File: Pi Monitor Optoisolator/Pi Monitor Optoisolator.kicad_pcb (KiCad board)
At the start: 2 copper layers, 38 x 38 mm, 15 parts, among them J1 Conn_01x07_Pin, J2 Conn_01x07_Pin, Q1 WL-OCPT_SERIES_827, Q2 WL-OCPT_SERIES_827, Q3 WL-OCPT_SERIES_827

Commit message: Minor adjustments
* Renamed LICENSE to COPYING (I wish GitHub would ask you what you wanted to name the license file)
* Added a COPYRIGHT NOTICE for the Pi Monitor Optoisolator. I did this as a seperate file, because unlike actual code files, there's not a ton of room for lots of text in a schematic or PCB drawing file.
* Update .gitignore file
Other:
- board text added: "Pi Monitor Optoisolator PCB v1.0 Part of mcu-on-the-go project https://github.com/jseyfert3/mcu-on-the-go"
- board text removed: "Pi Monitor Optoisolator Board v1.0 github.com/jseyfert3/"
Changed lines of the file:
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@@
 	)
 	(paper "A4")
+	(title_block
+		(title "Pi Monitor Optoisolator PCB")
+		(date "2025-07-18")
+		(rev "v1.0")
+		(comment 1 "See details at https://github.com/jseyfert3/mcu-on-the-go")
+		(comment 2 "Released under GPL-3.0-or-later license")
+		(comment 3 "Copyright 2025 Jonathan Seyfert")
+	)
 	(layers
 		(0 "F.Cu" signal)
@@
 		(property ki_fp_filters "R_*")
 		(sheetname "/")
-		(sheetfile "Pi_monitor.kicad_sch")
+		(sheetfile "Pi Monitor Optoisolator.kicad_sch")
 		(attr through_hole)
 		(fp_line
@@
 		(property ki_fp_filters "Connector*:*_1x??_*")
 		(sheetname "/")
-		(sheetfile "Pi_monitor.kicad_sch")
+		(sheetfile "Pi Monitor Optoisolator.kicad_sch")
 		(attr through_hole)
 		(fp_line
@@
 		)
 		(sheetname "/")
-		(sheetfile "Pi_monitor.kicad_sch")
+		(sheetfile "Pi Monitor Optoisolator.kicad_sch")
 		(attr through_hole)
 		(fp_line
@@
 		(property ki_fp_filters "Connector*:*_1x??_*")
 		(sheetname "/")
-		(sheetfile "Pi_monitor.kicad_sch")
+		(sheetfile "Pi Monitor Optoisolator.kicad_sch")
 		(attr through_hole)
 		(fp_line
@@
 		(property ki_fp_filters "R_*")
 		(sheetname "/")
-		(sheetfile "Pi_monitor.kicad_sch")
+		(sheetfile "Pi Monitor Optoisolator.kicad_sch")
 		(attr through_hole)
 		(fp_line
@@
 		)
 		(sheetname "/")
-		(sheetfile "Pi_monitor.kicad_sch")
+		(sheetfile "Pi Monitor Optoisolator.kicad_sch")
 		(attr through_hole)
 		(fp_line
@@
 		(property ki_fp_filters "R_*")
 		(sheetname "/")
-		(sheetfile "Pi_monitor.kicad_sch")
+		(sheetfile "Pi Monitor Optoisolator.kicad_sch")
 		(attr through_hole)
 		(fp_line
@@
 		)
 		(sheetname "/")
-		(sheetfile "Pi_monitor.kicad_sch")
+		(sheetfile "Pi Monitor Optoisolator.kicad_sch")
 		(attr through_hole)
 		(fp_line
@@
 		(property ki_fp_filters "R_*")
 		(sheetname "/")
-		(sheetfile "Pi_monitor.kicad_sch")
+		(sheetfile "Pi Monitor Optoisolator.kicad_sch")
 		(attr through_hole)
 		(fp_line
@@
 		(property ki_fp_filters "R_*")
 		(sheetname "/")
-		(sheetfile "Pi_monitor.kicad_sch")
+		(sheetfile "Pi Monitor Optoisolator.kicad_sch")
 		(attr through_hole)
 		(fp_line
@@
 		(property ki_fp_filters "R_*")
 		(sheetname "/")
-		(sheetfile "Pi_monitor.kicad_sch")
+		(sheetfile "Pi Monitor Optoisolator.kicad_sch")
 		(attr through_hole)
 		(fp_line
@@
 		(layer "Edge.Cuts")
 	)
-	(gr_text "Pi Monitor Optoisolator Board\nv1.0\n\ngithub.com/jseyfert3/"
-		(at 76.29 78.21 0)
+	(gr_text "Pi Monitor Optoisolator PCB\nv1.0\n\nPart of mcu-on-the-go project\nhttps://github.com/jseyfert3/mcu-on-the-go"
+		(at 84.74 79.01 0)
 		(layer "B.SilkS")
 		(effects
 			(font
 				(size 1 1)
-				(thickness 0.1)
+				(thickness 0.127)
 			)
 			(justify left bottom mirror)

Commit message: fix: Updated PN of optoisolator
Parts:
- Q1, Q2, Q3: value WL-OCPT_SERIES_827 -> 140827181010
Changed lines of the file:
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@@
 			)
 		)
-		(property "Value" "WL-OCPT_SERIES_827"
+		(property "Value" "140827181010"
 			(at 0 7.365 0)
 			(layer "F.Fab")
@@
 			)
 		)
-		(property "Value" "WL-OCPT_SERIES_827"
+		(property "Value" "140827181010"
 			(at 0 7.365 0)
 			(layer "F.Fab")
@@
 			)
 		)
-		(property "Value" "WL-OCPT_SERIES_827"
+		(property "Value" "140827181010"
 			(at 0 7.365 0)
 			(layer "F.Fab")

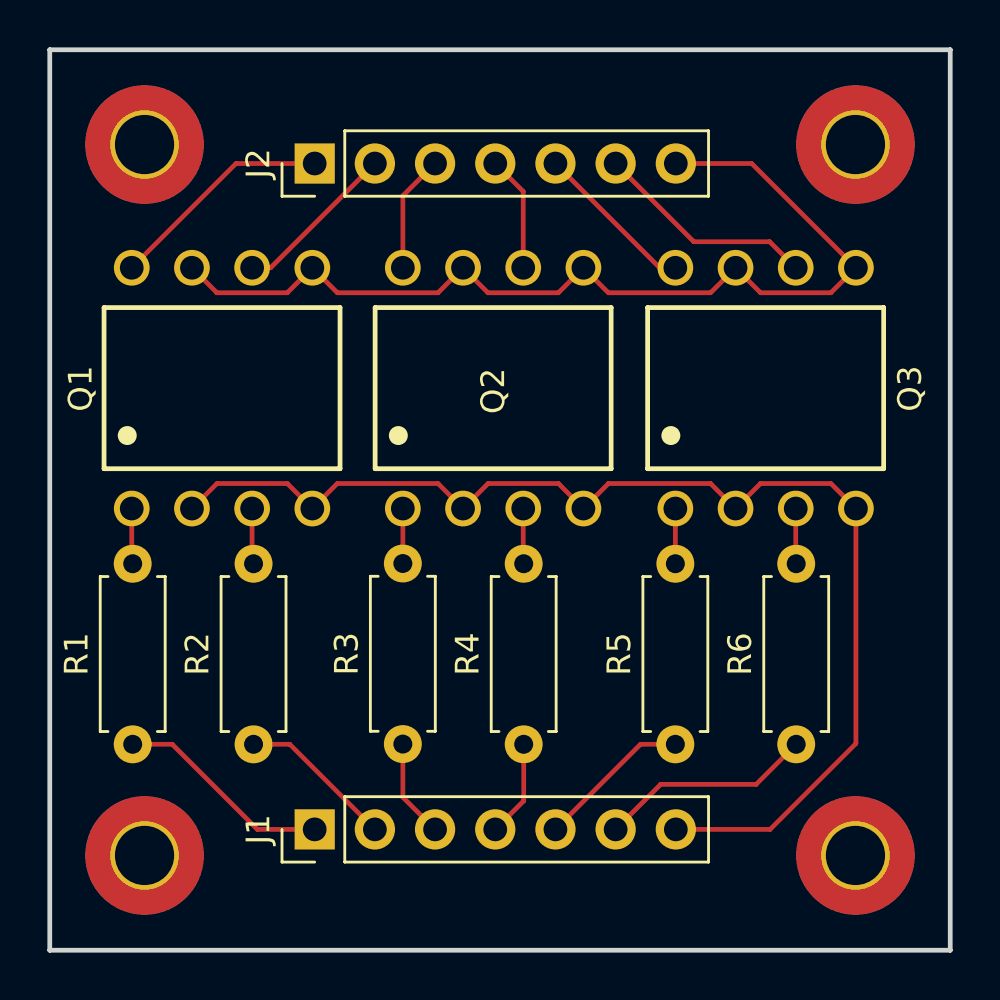
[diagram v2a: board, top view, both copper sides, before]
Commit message: feat: Shrunk edge cuts to save ~$1 at OSHPark
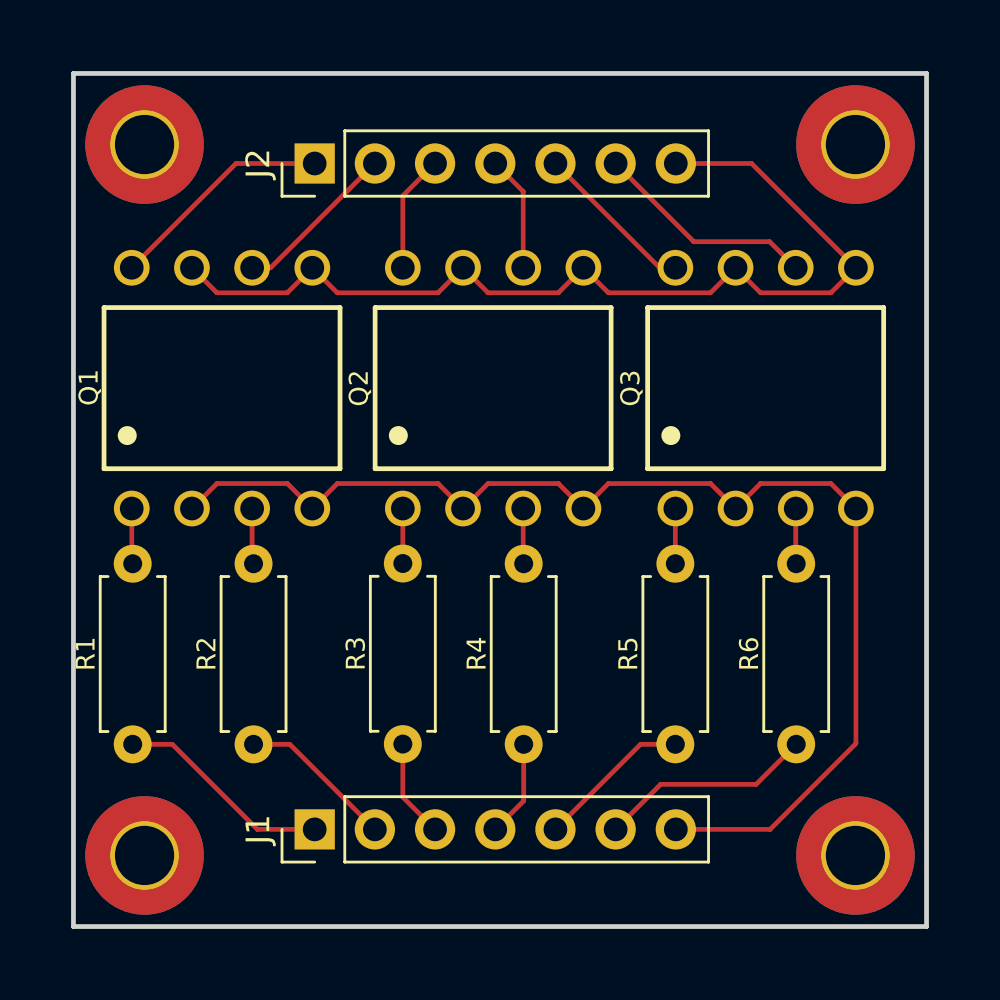
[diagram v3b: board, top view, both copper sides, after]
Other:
- board size 38 x 38 mm -> 36 x 36 mm
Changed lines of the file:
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@@
 		(tags "Resistor Axial_DIN0207 series Axial Horizontal pin pitch 7.62mm 0.25W = 1/4W length 6.3mm diameter 2.5mm")
 		(property "Reference" "R1"
-			(at 3.81 -2.37 90)
+			(at 3.82 -1.98 90)
 			(layer "F.SilkS")
 			(effects
 				(font
-					(size 1 1)
+					(size 0.8 0.8)
 					(thickness 0.15)
 				)
@@
 		(at 78.21 75.28)
 		(property "Reference" "Q3"
-			(at 6.09 0.02 90)
+			(at -5.7 0 90)
 			(layer "F.SilkS")
 			(effects
 				(font
-					(size 1 1)
+					(size 0.8 0.8)
 					(thickness 0.15)
 				)
@@
 		(tags "Resistor Axial_DIN0207 series Axial Horizontal pin pitch 7.62mm 0.25W = 1/4W length 6.3mm diameter 2.5mm")
 		(property "Reference" "R6"
-			(at 3.81 -2.37 90)
+			(at 3.82 -1.98 90)
 			(layer "F.SilkS")
 			(effects
 				(font
-					(size 1 1)
+					(size 0.8 0.8)
 					(thickness 0.15)
 				)
@@
 		(at 55.27 75.28)
 		(property "Reference" "Q1"
-			(at -5.97 0.02 90)
+			(at -5.62 -0.03 90)
 			(layer "F.SilkS")
 			(effects
 				(font
-					(size 1 1)
+					(size 0.8 0.8)
 					(thickness 0.15)
 				)
@@
 		(tags "Resistor Axial_DIN0207 series Axial Horizontal pin pitch 7.62mm 0.25W = 1/4W length 6.3mm diameter 2.5mm")
 		(property "Reference" "R2"
-			(at 3.81 -2.37 90)
+			(at 3.82 -1.98 90)
 			(layer "F.SilkS")
 			(effects
 				(font
-					(size 1 1)
+					(size 0.8 0.8)
 					(thickness 0.15)
 				)
@@
 		(at 66.71 75.28)
 		(property "Reference" "Q2"
-			(at 0 0.12 90)
+			(at -5.66 0 90)
 			(layer "F.SilkS")
 			(effects
 				(font
-					(size 1 1)
+					(size 0.8 0.8)
 					(thickness 0.15)
 				)
@@
 		(tags "Resistor Axial_DIN0207 series Axial Horizontal pin pitch 7.62mm 0.25W = 1/4W length 6.3mm diameter 2.5mm")
 		(property "Reference" "R3"
-			(at 3.81 -2.37 90)
+			(at 3.82 -1.98 90)
 			(layer "F.SilkS")
 			(effects
 				(font
-					(size 1 1)
+					(size 0.8 0.8)
 					(thickness 0.15)
 				)
@@
 		(tags "Resistor Axial_DIN0207 series Axial Horizontal pin pitch 7.62mm 0.25W = 1/4W length 6.3mm diameter 2.5mm")
 		(property "Reference" "R5"
-			(at 3.81 -2.37 90)
+			(at 3.82 -1.98 90)
 			(layer "F.SilkS")
 			(effects
 				(font
-					(size 1 1)
+					(size 0.8 0.8)
 					(thickness 0.15)
 				)
@@
 		(tags "Resistor Axial_DIN0207 series Axial Horizontal pin pitch 7.62mm 0.25W = 1/4W length 6.3mm diameter 2.5mm")
 		(property "Reference" "R4"
-			(at 3.81 -2.37 90)
+			(at 3.82 -1.98 90)
 			(layer "F.SilkS")
 			(effects
 				(font
-					(size 1 1)
+					(size 0.8 0.8)
 					(thickness 0.15)
 				)
@@
 	)
 	(gr_rect
-		(start 48 61)
-		(end 86 99)
+		(start 49 62)
+		(end 85 98)
 		(stroke
 			(width 0.2)
@@
 	)
 	(gr_text "Pi Monitor Optoisolator PCB\nv1.0\n\nPart of mcu-on-the-go project\nhttps://github.com/jseyfert3/mcu-on-the-go"
-		(at 84.74 79.01 0)
+		(at 85.04 79.25 0)
 		(layer "B.SilkS")
 		(effects
